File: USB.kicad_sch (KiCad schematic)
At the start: 13 parts, among them J401 USB_B_Micro, Q401 S8050, Q402 S8050, U401 CH340C, U402 RCLAMP0524P-N

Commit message: Rename Ferrite_Bead to FerriteBead
Symbol name changed between KiCad 5 and 6...
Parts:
- FB401: symbol Device:Ferrite_Bead -> Device:FerriteBead
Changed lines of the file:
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@@
     (pin "9")
   )
-  (symbol (lib_id "Device:Ferrite_Bead") (at 67.31 39.37 270) (unit 1)
+  (symbol (lib_id "Device:FerriteBead") (at 67.31 39.37 270) (unit 1)
     (in_bom yes) (on_board yes)
     (property "Reference" "FB401" (id 0) (at 67.31 32.4104 90))

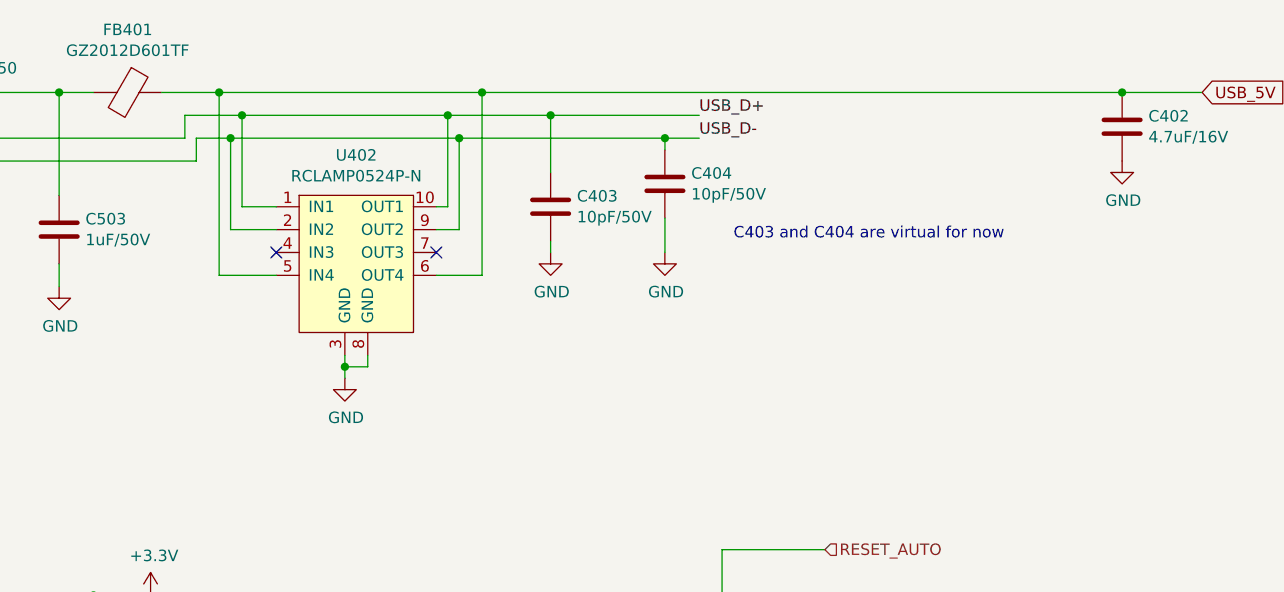
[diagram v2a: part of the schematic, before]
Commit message: Improve connector ESD protection; bump version to 2.0.2
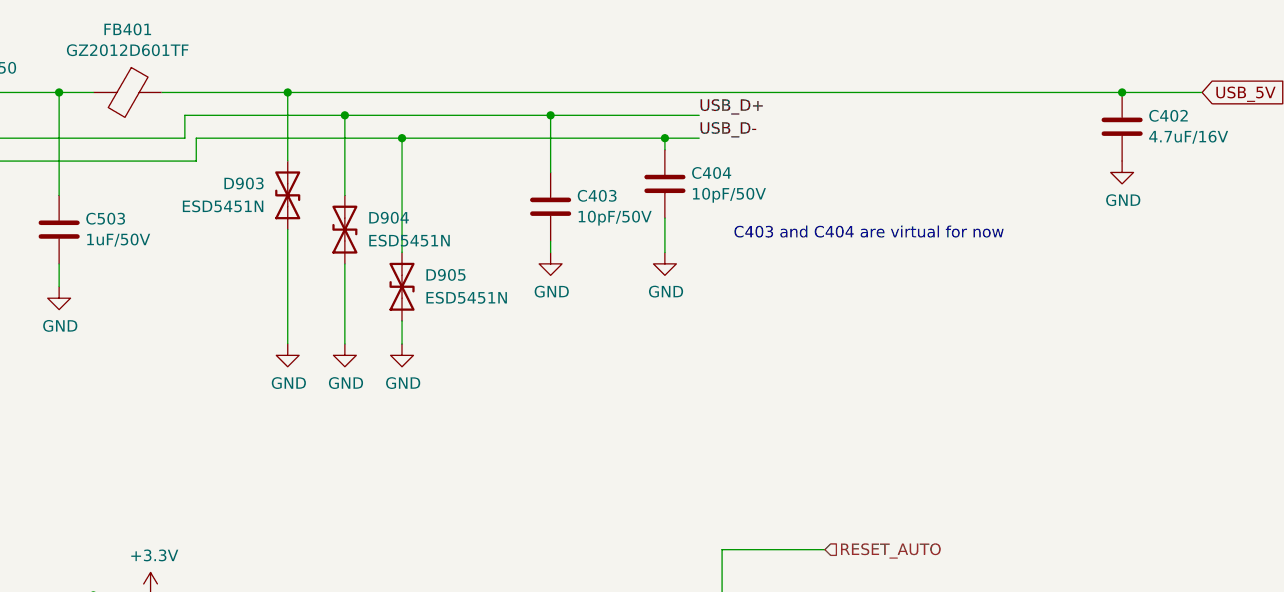
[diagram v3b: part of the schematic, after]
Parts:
- removed U402: RCLAMP0524P-N, Package_DFN_QFN:Diodes_UDFN-10_1.0x2.5mm_P0.5mm, symbol SH-ESP32:RCLAMP0524P-N
- added D903, D904, D905: ESD5451N, Diode_SMD:D_0402_1005Metric, symbol Device:D_TVS
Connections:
- net GND: now also D903.1 (A1), D904.1 (A1), D905.1 (A1)
- net USB_5V: now also D903.2 (A2)
- net USB_D+: now also D904.2 (A2)
- net USB_D-: now also D905.2 (A2)
- no-connect marks 8 -> 6

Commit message: Save schema with KiCad 7.0.6
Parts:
- Q401, Q402, U401: JLCPCB_CORRECTION (none) -> 0;0;180

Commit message: Fix component rotations
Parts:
- J401: JLCPCB_CORRECTION (none) -> 1.3;0.5;0
- U401: JLCPCB_CORRECTION 0;0;180 -> 0;0;270
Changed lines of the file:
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@@
       (effects (font (size 1.27 1.27)) hide)
     )
-    (property "JLCPCB_CORRECTION" "" (at 25.4 44.45 0)
+    (property "JLCPCB_CORRECTION" "1.3;0.5;0" (at 25.4 44.45 0)
       (effects (font (size 1.27 1.27)) hide)
     )
@@
       (effects (font (size 1.27 1.27)) hide)
     )
-    (property "JLCPCB_CORRECTION" "0;0;180" (at 52.07 127 0)
+    (property "JLCPCB_CORRECTION" "0;0;270" (at 52.07 127 0)
       (effects (font (size 1.27 1.27)) hide)
     )

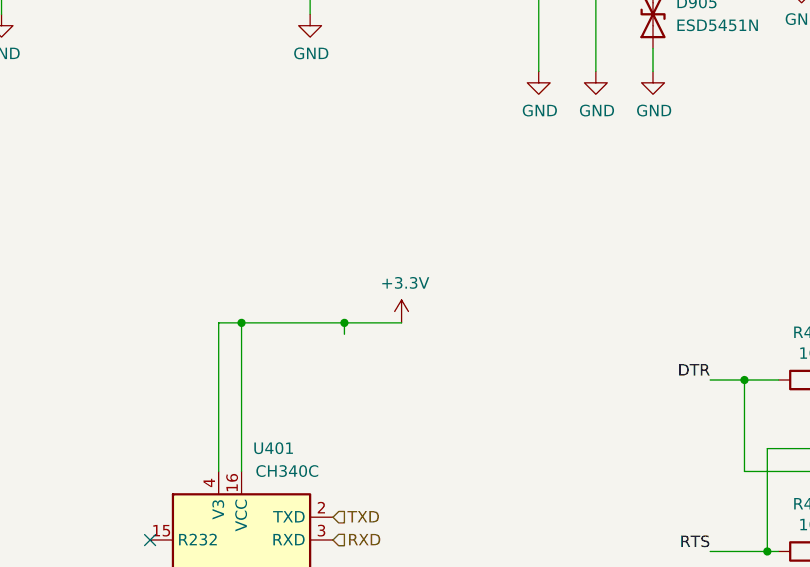
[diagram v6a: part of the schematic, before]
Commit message: Go back to ISO1050 for CAN transceiver
Also add CAN RX and TX LEDs and beef up buck capacitors
as much as space allows.
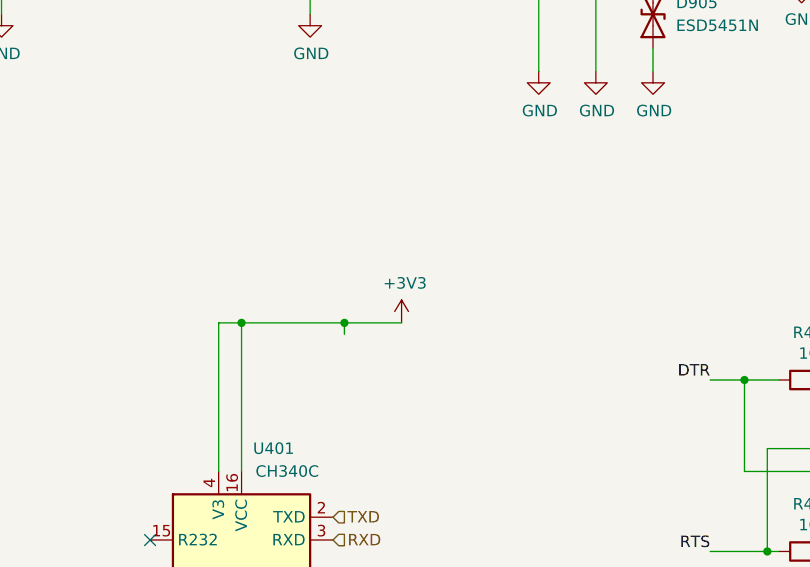
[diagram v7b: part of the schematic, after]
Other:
- company: Hat Labs Ltd -> Hat Labs Oy
- title: Sailor Hat with ESP32 -> SH-ESP32

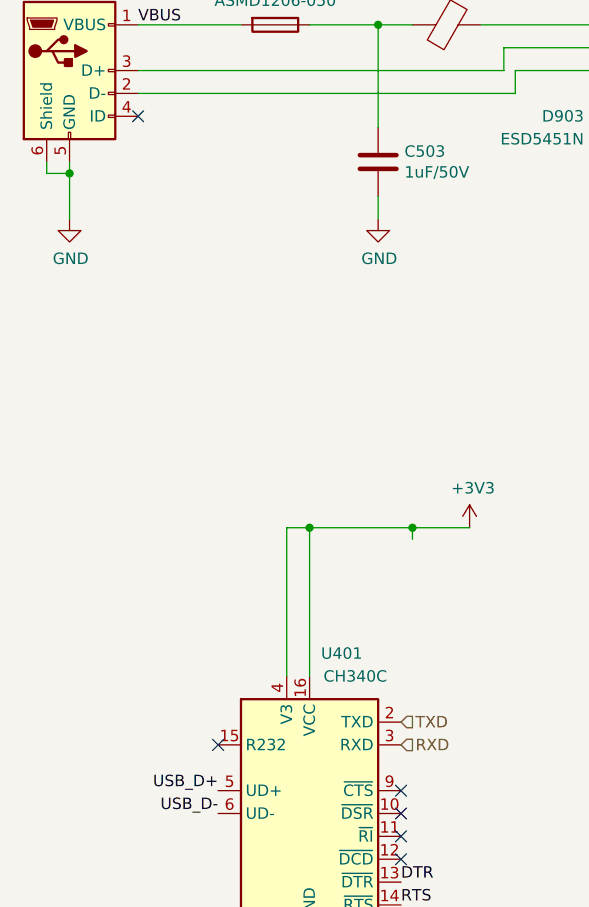
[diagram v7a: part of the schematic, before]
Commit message: Change buck converter to LMR54410
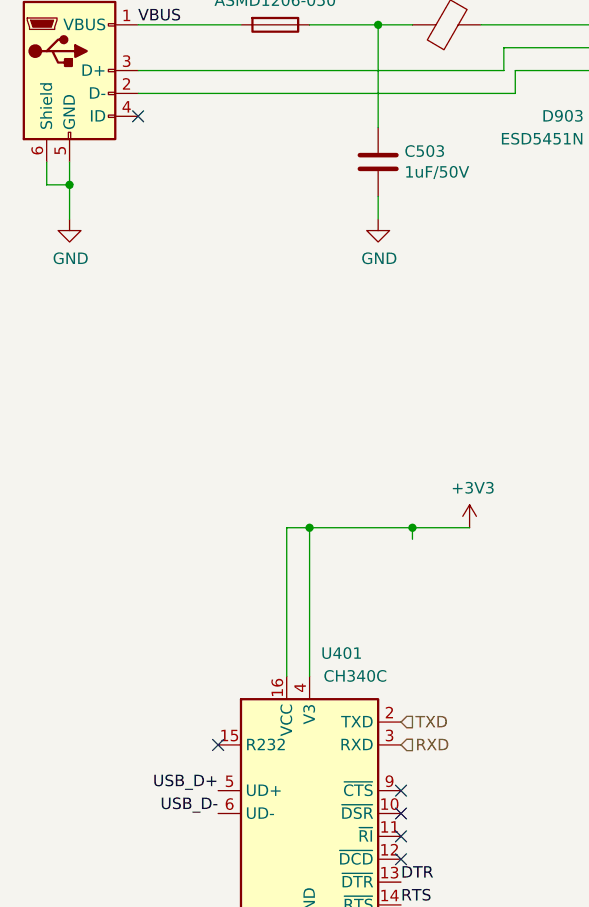
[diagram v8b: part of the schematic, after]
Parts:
- Q401, Q402: footprint Package_TO_SOT_SMD:SOT-23 -> SH-ESP32:SOT-23
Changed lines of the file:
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@@
 	(title_block
 		(title "SH-ESP32")
-		(date "2024-06-27")
-		(rev "2.1.0")
+		(date "2024-09-24")
+		(rev "2.2.0")
 		(company "Hat Labs Oy")
 		(comment 1 "https://creativecommons.org/licenses/by-sa/4.0")
@@
 	)
 	(junction
-		(at 25.4 55.88)
+		(at 25.4 57.15)
 		(diameter 0)
 		(color 0 0 0 0)
@@
 	(wire
 		(pts
-			(xy 22.86 55.88) (xy 22.86 54.61)
+			(xy 22.86 57.15) (xy 22.86 54.61)
 		)
 		(stroke
@@
 	(wire
 		(pts
-			(xy 25.4 54.61) (xy 25.4 55.88)
+			(xy 25.4 54.61) (xy 25.4 57.15)
 		)
 		(stroke
@@
 	(wire
 		(pts
-			(xy 22.86 55.88) (xy 25.4 55.88)
+			(xy 22.86 57.15) (xy 25.4 57.15)
 		)
 		(stroke
@@
 	(wire
 		(pts
-			(xy 25.4 55.88) (xy 25.4 60.96)
+			(xy 25.4 57.15) (xy 25.4 60.96)
 		)
 		(stroke
@@
 			)
 		)
-		(property "Description" ""
+		(property "Description" "Power symbol creates a global label with name \"GND\" , ground"
 			(at 25.4 60.96 0)
 			(effects
@@
 			)
 		)
-		(property "Description" ""
+		(property "Description" "USB serial converter, crystal-less, UART, SOIC-16"
 			(at 52.07 127 0)
 			(effects
@@
 			)
 		)
-		(property "Footprint" "Package_TO_SOT_SMD:SOT-23"
+		(property "Footprint" "SH-ESP32:SOT-23"
 			(at 135.89 103.505 0)
 			(effects
@@
 			)
 		)
-		(property "Description" ""
+		(property "Description" "0.7A Ic, 20V Vce, Low Voltage High Current NPN Transistor, SOT-23"
 			(at 130.81 101.6 0)
 			(effects
@@
 			)
 		)
-		(property "Footprint" "Package_TO_SOT_SMD:SOT-23"
+		(property "Footprint" "SH-ESP32:SOT-23"
 			(at 135.89 118.745 0)
 			(effects
@@
 			)
 		)
-		(property "Description" ""
+		(property "Description" "0.7A Ic, 20V Vce, Low Voltage High Current NPN Transistor, SOT-23"
 			(at 130.81 120.65 0)
 			(effects
@@
 			)
 		)
-		(property "Description" ""
+		(property "Description" "Power symbol creates a global label with name \"GND\" , ground"
 			(at 177.8 46.99 0)
 			(effects
@@
 			)
 		)
-		(property "Description" ""
+		(property "Description" "Power symbol creates a global label with name \"GND\" , ground"
 			(at 52.07 142.24 0)
 			(effects
@@
 			)
 		)
-		(property "Description" ""
+		(property "Description" "Power symbol creates a global label with name \"GND\" , ground"
 			(at 114.3 57.15 0)
 			(effects
@@
 			)
 		)
-		(property "Description" ""
+		(property "Description" "Power symbol creates a global label with name \"GND\" , ground"
 			(at 127 57.15 0)
 			(effects
@@
 			)
 		)
-		(property "Description" ""
+		(property "Description" "Power symbol creates a global label with name \"+3.3V\""
 			(at 69.85 95.25 0)
 			(effects
@@
 			)
 		)
-		(property "Description" ""
+		(property "Description" "Power symbol creates a global label with name \"GND\" , ground"
 			(at 59.69 60.96 0)
 			(effects
@@
 			)
 		)
-		(property "Description" ""
+		(property "Description" "Power symbol creates a global label with name \"GND\" , ground"
 			(at 97.79 67.31 0)
 			(effects
@@
 			)
 		)
-		(property "Description" ""
+		(property "Description" "Power symbol creates a global label with name \"GND\" , ground"
 			(at 85.09 67.31 0)
 			(effects
@@
 			)
 		)
-		(property "Description" ""
+		(property "Description" "Power symbol creates a global label with name \"GND\" , ground"
 			(at 91.44 67.31 0)
 			(effects
